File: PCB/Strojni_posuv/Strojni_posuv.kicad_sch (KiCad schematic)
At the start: 63 parts, among them J1 Conn_01x20_Pin, J10 Button_right_A, J11 Button_left_fast_A, J12 Button_right_fast_A, J13 Button_left_fast_B, J14 Button_right_fast_B, J15 Conn_01x06_Socket, J7 Button_left_A, J8 Button_left_B, J9 Button_right_A, SW2 SW_DPST_x2, SW3 SW_DPST_x2, SW4 SW_SPDT, SW5 RotaryEncoder_Switch, U1 STM32F103RBTx, Y1 16MHz

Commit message: Revision 0 - final
I send this files to JLCPCB
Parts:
- C5: LCSC C307517 -> C15850
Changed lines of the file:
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@@
 			)
 		)
-		(property "LCSC" "C307517"
+		(property "LCSC" "C15850"
 			(at 67.31 22.86 0)
 			(effects

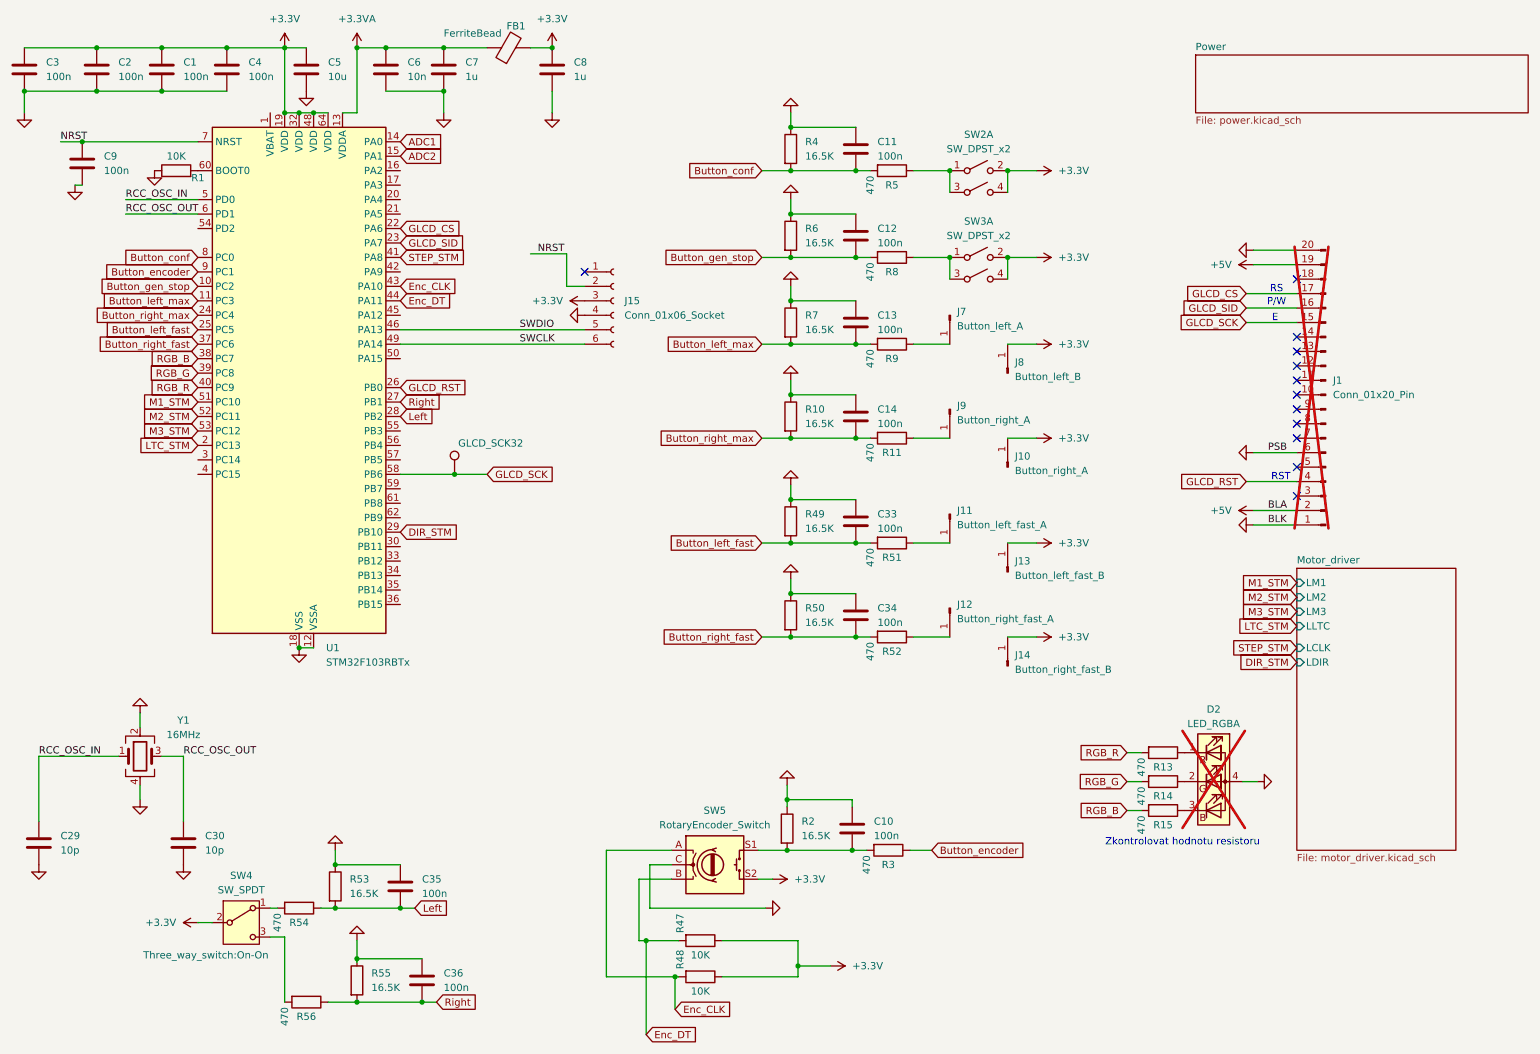
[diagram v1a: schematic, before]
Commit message: Starting new Revision 1
addressing some problems and mistakes
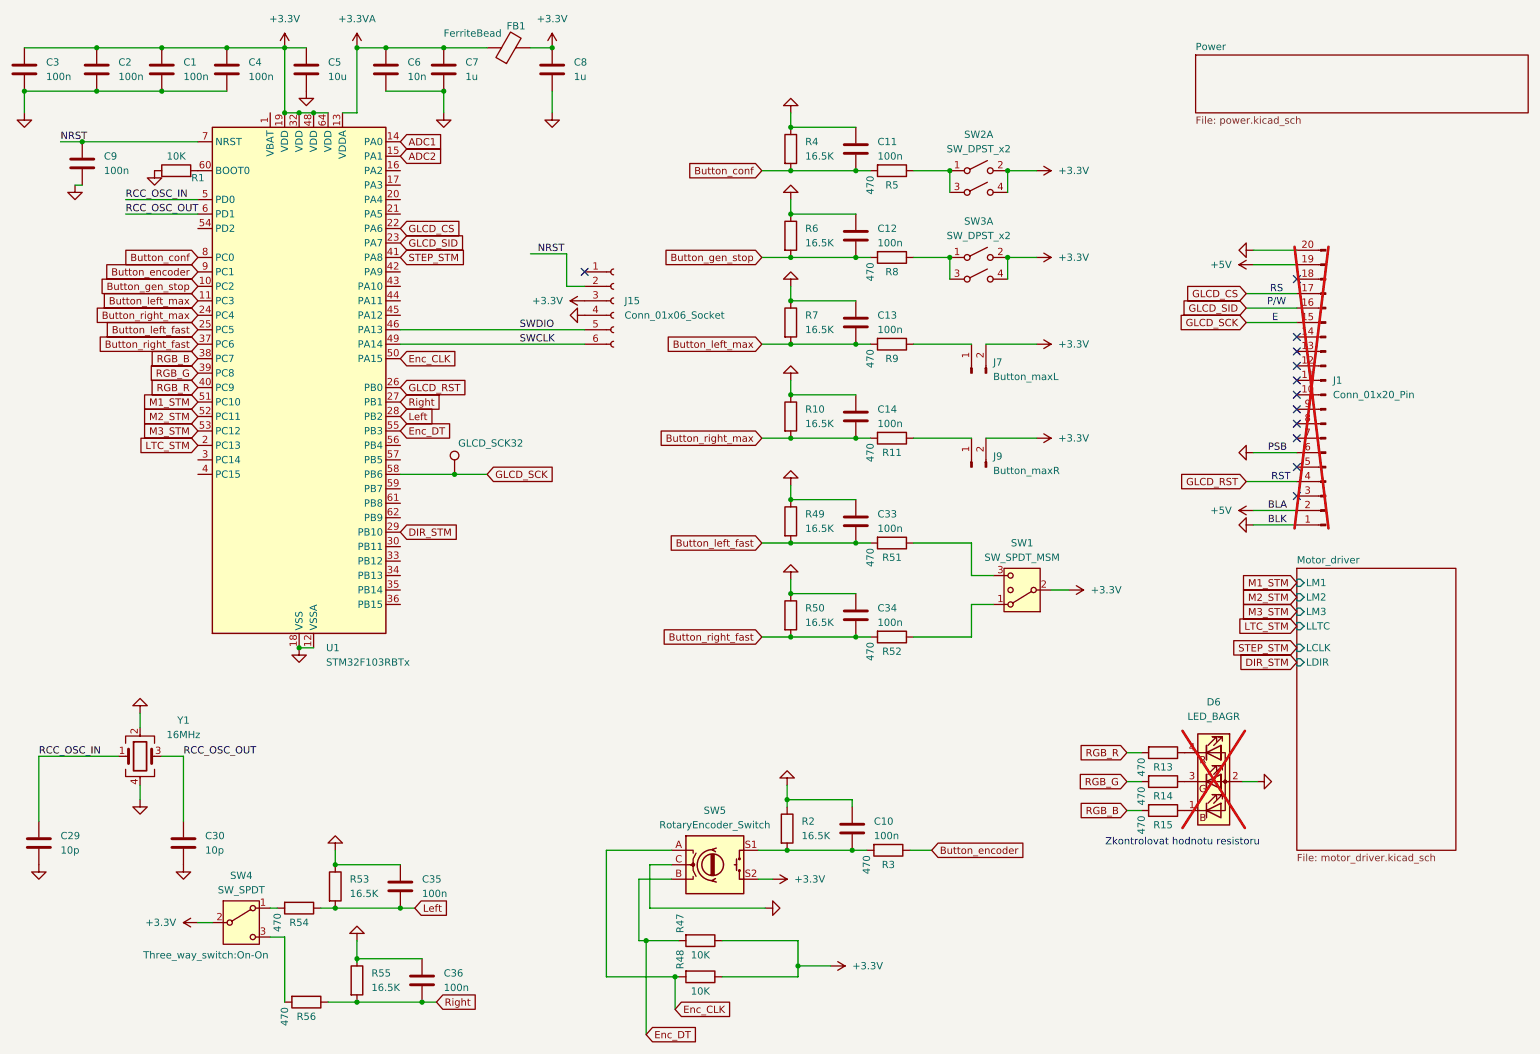
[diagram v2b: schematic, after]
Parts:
- removed D2: LED_RGBA, LED_THT:LED_D5.0mm-4_RGB_Wide_Pins, symbol Device:LED_RGBA
- removed J10, J9: Button_right_A, Connector_Pin:Pin_D1.3mm_L11.3mm_W2.8mm_Flat, symbol Connector:Conn_01x01_Pin
- removed J11: Button_left_fast_A, Connector_Pin:Pin_D1.3mm_L11.3mm_W2.8mm_Flat, symbol Connector:Conn_01x01_Pin
- removed J12: Button_right_fast_A, Connector_Pin:Pin_D1.3mm_L11.3mm_W2.8mm_Flat, symbol Connector:Conn_01x01_Pin
- removed J13: Button_left_fast_B, Connector_Pin:Pin_D1.3mm_L11.3mm_W2.8mm_Flat, symbol Connector:Conn_01x01_Pin
- removed J14: Button_right_fast_B, Connector_Pin:Pin_D1.3mm_L11.3mm_W2.8mm_Flat, symbol Connector:Conn_01x01_Pin
- removed J7: Button_left_A, Connector_Pin:Pin_D1.3mm_L11.3mm_W2.8mm_Flat, symbol Connector:Conn_01x01_Pin
- removed J8: Button_left_B, Connector_Pin:Pin_D1.3mm_L11.3mm_W2.8mm_Flat, symbol Connector:Conn_01x01_Pin
- added D6: LED_BAGR, LED_THT:LED_D5.0mm-4_RGB_Wide_Pins, symbol Device:LED_BAGR
- added J7: Button_maxL, Connector_JST:JST_XH_B2B-XH-A_1x02_P2.50mm_Vertical, symbol Connector:Conn_01x02_Pin
- added J9: Button_maxR, Connector_JST:JST_XH_B2B-XH-A_1x02_P2.50mm_Vertical, symbol Connector:Conn_01x02_Pin
- added SW1: SW_SPDT_MSM, Button_Switch_THT:SW_CK_JS202011CQN_DPDT_Straight, symbol Switch:SW_SPDT_MSM
- C5: footprint Capacitor_SMD:C_0805_2012Metric -> Capacitor_SMD:C_0603_1608Metric
- R1, R10, R11, R13, R14, R15, R2, R3, R4, R47, R48, R49, R5, R50, R51, R52, R53, R54, R55, R56, R6, R7, R8, R9: footprint Resistor_SMD:R_0603_1608Metric -> Resistor_SMD:R_0805_2012Metric
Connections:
- net +3.3V: now also J7.2 (Pin_2), J9.2 (Pin_2), SW1.2 (3)
- net Enc_CLK: now also U1.50 (PA15); no longer U1.43 (PA10)
- net Enc_DT: now also U1.55 (PB3); no longer U1.44 (PA11)
- net GND: now also D6.2 (A)
- net at R15.1: now also D6.1 (BK)
- net at R13.1: now also D6.4 (RK)
- net at R14.1: now also D6.3 (GK)
- net at R51.1: now also SW1.3 (4)
- net at R52.1: now also SW1.1
- net at R9.1: now also J7.1 (Pin_1)
- net at R11.1: now also J9.1 (Pin_1)

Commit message: Resolving problems from list
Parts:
- removed C12: 100n, Capacitor_SMD:C_0603_1608Metric, symbol Device:C
- removed J15: Conn_01x06_Socket, Connector_PinSocket_2.54mm:PinSocket_1x06_P2.54mm_Vertical, symbol Connector:Conn_01x06_Socket
- removed R6: 16.5K, Resistor_SMD:R_0805_2012Metric, symbol Device:R
- removed R8: 470, Resistor_SMD:R_0805_2012Metric, symbol Device:R
- removed SW3: SW_DPST_x2, Button_Switch_THT:SW_PUSH_6mm, symbol Switch:SW_DPST_x2
- added J10: Conn_01x05_Socket, Connector_JST:JST_PH_B5B-PH-K_1x05_P2.00mm_Vertical, symbol Connector:Conn_01x05_Socket
- added J8: Volne_IO, symbol Connector:Conn_01x06_Pin
- SW1: footprint Button_Switch_THT:SW_CK_JS202011CQN_DPDT_Straight -> ON_Off_ON:on_off_on
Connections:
- net +3.3V: now also J10.2 (Pin_2), J8.6 (Pin_6)
- net GND: now also J10.3 (Pin_3), J8.5 (Pin_5)
- net NRST: now also J10.1 (Pin_1)
- net SWCLK: now also J10.5 (Pin_5)
- net SWDIO: now also J10.4 (Pin_4)
- net PA2: now reaches U1.16 (PA2)
- net PA2: now also J8.1 (Pin_1)
- net PA9: now reaches U1.42 (PA9)
- net PA9: now also J8.2 (Pin_2)
- net PB4: now reaches U1.56 (PB4)
- net PB4: now also J8.3 (Pin_3)
- net PB5: now reaches U1.57 (PB5)
- net PB5: now also J8.4 (Pin_4)
- net Button_gen_stop: no longer names the net of U1.10 (PC2)
- no-connect marks 12 -> 11
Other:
- moved on the sheet: C11, R4, R5, SW2A

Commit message: Schema done?
I think that I have functional schema, but it needs a check
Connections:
- net Enable: now reaches U1.33 (PB12)
- net Reset: now reaches U1.35 (PB14)
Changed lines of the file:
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@@
+		)
+	)
+	(global_label "Reset"
+		(shape input)
+		(at 83.82 114.3 0)
+		(fields_autoplaced yes)
+		(effects
+			(font
+				(size 1.27 1.27)
+			)
+			(justify left)
+		)
+		(property "Intersheetrefs" "${INTERSHEET_REFS}"
+			(at 92.0062 114.3 0)
+			(effects
+				(font
+					(size 1.27 1.27)
+				)
+				(justify left)
+				(hide yes)
+			)
 		)
 	)
@@
 				(hide yes)
 			)
+		)
+	)
+	(global_label "Enable"
+		(shape input)
+		(at 83.82 109.22 0)
+		(fields_autoplaced yes)
+		(effects
+			(font
+				(size 1.27 1.27)
+			)
+			(justify left)
+		)
+		(property "Intersheetrefs" "${INTERSHEET_REFS}"
+			(at 93.155 109.22 0)
+			(effects
+				(font
+					(size 1.27 1.27)
+				)
+				(justify left)
+				(hide yes)
+			)

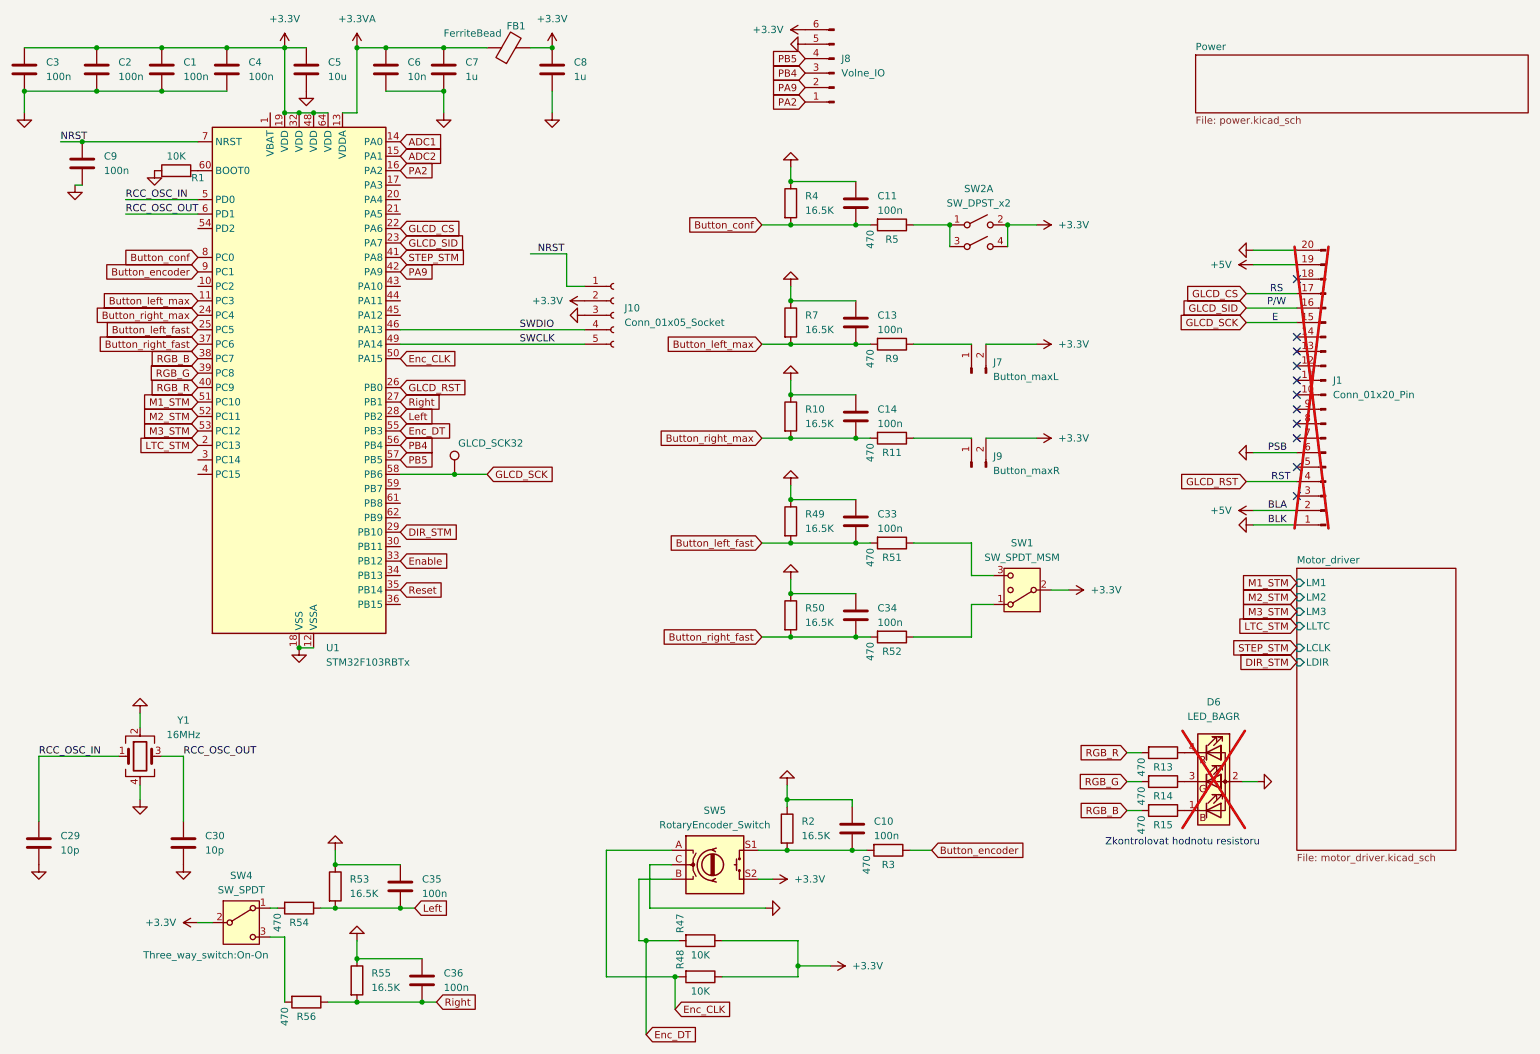
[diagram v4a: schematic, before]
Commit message: PCB done?
I did all the routing and component placement on PCB
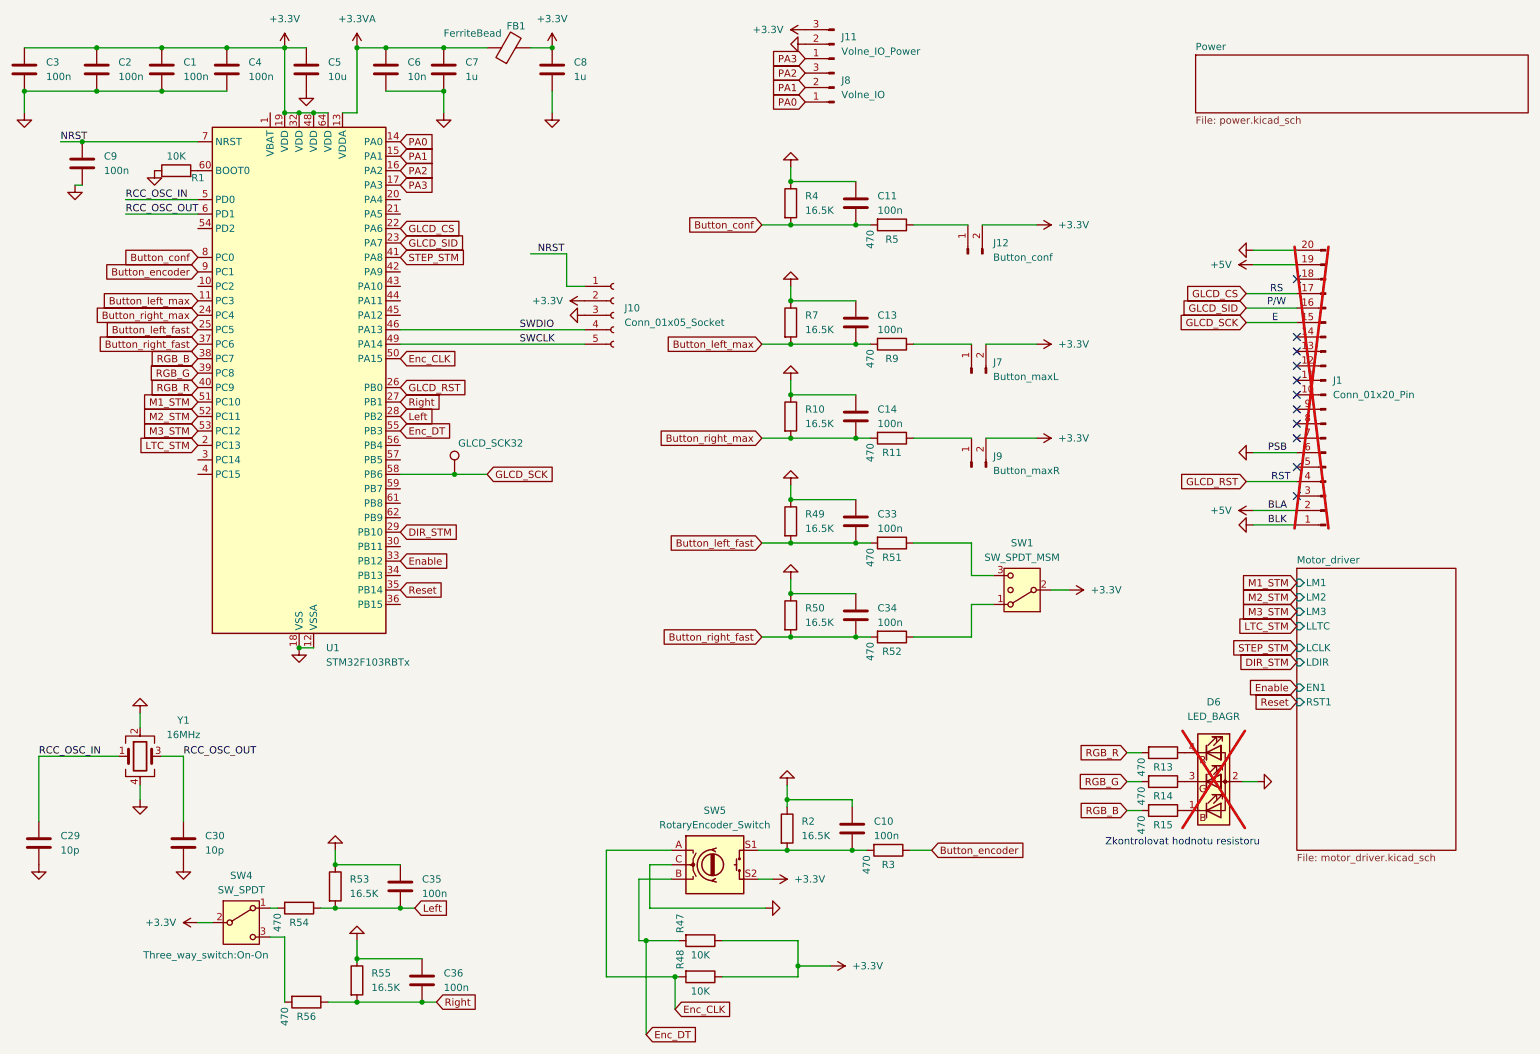
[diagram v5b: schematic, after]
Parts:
- removed J8: Volne_IO, symbol Connector:Conn_01x06_Pin
- removed SW2: SW_DPST_x2, Button_Switch_THT:SW_PUSH_6mm, symbol Switch:SW_DPST_x2
- added J11: Volne_IO_Power, TerminalBlock:TerminalBlock_Xinya_XY308-2.54-3P_1x03_P2.54mm_Horizontal, symbol Connector:Conn_01x03_Pin
- added J12: Button_conf, Connector_JST:JST_XH_B2B-XH-A_1x02_P2.50mm_Vertical, symbol Connector:Conn_01x02_Pin
- added J8: Volne_IO, TerminalBlock:TerminalBlock_Xinya_XY308-2.54-3P_1x03_P2.54mm_Horizontal, symbol Connector:Conn_01x03_Pin
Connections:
- net +3.3V: now also J11.3 (Pin_3), J12.2 (Pin_2)
- net GND: now also J11.2 (Pin_2)
- net PA2: now also J8.3 (Pin_3)
- net at R5.1: now also J12.1 (Pin_1)
- net PA3: now reaches U1.17 (PA3)
- net PA3: now also J11.1 (Pin_1)
- net ADC1 renamed PA0
- net PA0: now also J8.1 (Pin_1)
- net ADC2 renamed PA1
- net PA1: now also J8.2 (Pin_2)
- net PA9: no longer names the net of U1.42 (PA9)
- net PB4: no longer names the net of U1.56 (PB4)
- net PB5: no longer names the net of U1.57 (PB5)
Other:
- sheet Motor_driver ports: added EN1, RST1; removed none
